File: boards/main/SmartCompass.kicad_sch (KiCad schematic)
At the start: 21 parts, among them J1 SWD HEADER, J2 EXPANSION, U1 BMD-340-A-R, U2 S25FL064LABNFI043, X1 USB4085-GF-A, Y1 32.768KHZ

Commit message: Fix missing/incorrect digikey numbers
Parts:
- R3, R5: DigiKey_PN (none) -> 311-27.0HRCT-ND
- R6, R7: DigiKey_PN (none) -> 311-4.70KHRCT-ND
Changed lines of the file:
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@@
 			)
 		)
+    (property "DigiKey_PN" "311-4.70KHRCT-ND" (at 128.27 92.71 0)
+      (effects (font (size 1.27 1.27)) (hide yes))
+    )
 		(pin "1"
 		)
@@
 			)
 		)
+    (property "DigiKey_PN" "311-27.0HRCT-ND" (at 254.0 77.47 0)
+      (effects (font (size 1.27 1.27)) (hide yes))
+    )
 		(pin "2"
 		)
@@
 			)
 		)
+    (property "DigiKey_PN" "311-4.70KHRCT-ND" (at 128.27 95.25 0)
+      (effects (font (size 1.27 1.27)) (hide yes))
+    )
 		(pin "1"
 		)
@@
 			)
 		)
+    (property "DigiKey_PN" "311-27.0HRCT-ND" (at 254.0 82.55 0)
+      (effects (font (size 1.27 1.27)) (hide yes))
+    )
 		(pin "2"
 		)

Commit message: Use proper flash footprint and model. Also swap out deprecated resistor on the main board
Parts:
- R1, R2, R4: DigiKey_PN 311-5.10KHRCT-ND -> P5.10KHCT-ND; MPN RC0603FR-075K1L -> ERJ-3EKF5101V; Manufacturer YAGEO -> Panasonic
- U2: footprint Package_DFN_QFN:DFN-8-1EP_4x4mm_P0.8mm_EP2.3x3.24mm -> smart_compass:SON80P400X400X60-9N
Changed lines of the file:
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@@
 			)
 		)
-		(property "Datasheet" "https://yageogroup.com/content/datasheet/asset/file/PYU-RC_GROUP_51_ROHS_L"
+		(property "Datasheet" "https://industrial.panasonic.com/cdbs/www-data/pdf/RDA0000/AOA0000C304.pdf"
 			(at 256.54 68.58 0)
 			(hide yes)
@@
 			)
 		)
-		(property "MPN" "RC0603FR-075K1L"
+		(property "MPN" "ERJ-3EKF5101V"
 			(at 256.54 68.58 0)
 			(hide yes)
@@
 			)
 		)
-		(property "Manufacturer" "YAGEO"
+		(property "Manufacturer" "Panasonic"
 			(at 256.54 68.58 0)
 			(hide yes)
@@
 			)
 		)
-		(property "DigiKey_PN" "311-5.10KHRCT-ND"
+		(property "DigiKey_PN" "P5.10KHCT-ND"
 			(at 256.54 68.58 0)
 			(hide yes)
@@
 			)
 		)
-    (property "DigiKey_PN" "311-4.70KHRCT-ND" (at 128.27 92.71 0)
-      (effects (font (size 1.27 1.27)) (hide yes))
-    )
+		(property "DigiKey_PN" "311-4.70KHRCT-ND"
+			(at 128.27 92.71 0)
+			(hide yes)
+			(show_name no)
+			(do_not_autoplace no)
+			(effects
+				(font
+					(size 1.27 1.27)
+				)
+			)
+		)
 		(pin "1"
 		)
@@
 			)
 		)
-    (property "DigiKey_PN" "311-27.0HRCT-ND" (at 254.0 77.47 0)
-      (effects (font (size 1.27 1.27)) (hide yes))
-    )
+		(property "DigiKey_PN" "311-27.0HRCT-ND"
+			(at 254 77.47 0)
+			(hide yes)
+			(show_name no)
+			(do_not_autoplace no)
+			(effects
+				(font
+					(size 1.27 1.27)
+				)
+			)
+		)
 		(pin "2"
 		)
@@
 			)
 		)
-		(property "Datasheet" "https://yageogroup.com/content/datasheet/asset/file/PYU-RC_GROUP_51_ROHS_L"
+		(property "Datasheet" "https://industrial.panasonic.com/cdbs/www-data/pdf/RDA0000/AOA0000C304.pdf"
 			(at 203.2 82.55 0)
 			(hide yes)
@@
 			)
 		)
-		(property "MPN" "RC0603FR-075K1L"
+		(property "MPN" "ERJ-3EKF5101V"
 			(at 203.2 82.55 0)
 			(hide yes)
@@
 			)
 		)
-		(property "Manufacturer" "YAGEO"
+		(property "Manufacturer" "Panasonic"
 			(at 203.2 82.55 0)
 			(hide yes)
@@
 			)
 		)
-		(property "DigiKey_PN" "311-5.10KHRCT-ND"
+		(property "DigiKey_PN" "P5.10KHCT-ND"
 			(at 203.2 82.55 0)
 			(hide yes)
@@
 			)
 		)
-		(property "Manufacturer" "Abracon"
-			(at 54.61 50.8 0)
-			(hide yes)
-			(show_name no)
-			(do_not_autoplace no)
-			(effects
-				(font
-					(size 1.27 1.27)
-				)
-				(justify bottom)
-			)
-		)
 		(property "MPN" "ABS07-32.768KHZ-7-T"
 			(at 54.61 50.8 90)
@@
 			)
 		)
-    (property "DigiKey_PN" "311-4.70KHRCT-ND" (at 128.27 95.25 0)
-      (effects (font (size 1.27 1.27)) (hide yes))
-    )
+		(property "DigiKey_PN" "311-4.70KHRCT-ND"
+			(at 128.27 95.25 0)
+			(hide yes)
+			(show_name no)
+			(do_not_autoplace no)
+			(effects
+				(font
+					(size 1.27 1.27)
+				)
+			)
+		)
 		(pin "1"
 		)
@@
 			)
 		)
-		(property "Datasheet" "https://yageogroup.com/content/datasheet/asset/file/PYU-RC_GROUP_51_ROHS_L"
+		(property "Datasheet" "https://industrial.panasonic.com/cdbs/www-data/pdf/RDA0000/AOA0000C304.pdf"
 			(at 256.54 71.12 0)
 			(hide yes)
@@
 			)
 		)
-		(property "MPN" "RC0603FR-075K1L"
+		(property "MPN" "ERJ-3EKF5101V"
 			(at 256.54 71.12 0)
 			(hide yes)
@@
 			)
 		)
-		(property "Manufacturer" "YAGEO"
+		(property "Manufacturer" "Panasonic"
 			(at 256.54 71.12 0)
 			(hide yes)
@@
 			)
 		)
-		(property "DigiKey_PN" "311-5.10KHRCT-ND"
+		(property "DigiKey_PN" "P5.10KHCT-ND"
 			(at 256.54 71.12 0)
 			(hide yes)
@@
 			)
 		)
-		(property "Footprint" "Package_DFN_QFN:DFN-8-1EP_4x4mm_P0.8mm_EP2.3x3.24mm"
+		(property "Footprint" "smart_compass:SON80P400X400X60-9N"
 			(at 248.92 146.05 0)
 			(hide yes)
@@
 			)
 		)
-		(property "Manufacturer" "Infineon Technologies"
-			(at 248.92 146.05 0)
-			(hide yes)
-			(show_name no)
-			(do_not_autoplace no)
-			(effects
-				(font
-					(size 1.27 1.27)
-				)
-				(justify bottom)
-			)
-		)
 		(property "MPN" "S25FL064LABNFI043"
 			(at 248.92 146.05 0)
@@
 			)
 		)
-    (property "DigiKey_PN" "311-27.0HRCT-ND" (at 254.0 82.55 0)
-      (effects (font (size 1.27 1.27)) (hide yes))
-    )
+		(property "DigiKey_PN" "311-27.0HRCT-ND"
+			(at 254 82.55 0)
+			(hide yes)
+			(show_name no)
+			(do_not_autoplace no)
+			(effects
+				(font
+					(size 1.27 1.27)
+				)
+			)
+		)
 		(pin "2"
 		)

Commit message: Grab missing footprints and models, and assign them to symbols
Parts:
- U1: footprint (none) -> smart_compass:RIGADO_BMD-340-A-R
- X1: footprint (none) -> smart_compass:GCT_USB4085-GF-A_REVA4
- Y1: footprint (none) -> smart_compass:XTAL_ABS07-32.768KHZ-7-T
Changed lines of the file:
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@@
 			)
 		)
-		(property "Footprint" ""
+		(property "Footprint" "smart_compass:RIGADO_BMD-340-A-R"
 			(at 97.79 69.85 0)
 			(hide yes)
@@
 			)
 		)
-		(property "Footprint" ""
+		(property "Footprint" "smart_compass:XTAL_ABS07-32.768KHZ-7-T"
 			(at 54.61 50.8 0)
 			(hide yes)
@@
 			)
 		)
-		(property "Footprint" ""
+		(property "Footprint" "smart_compass:GCT_USB4085-GF-A_REVA4"
 			(at 236.22 82.55 0)
 			(hide yes)

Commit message: replace capacitor that's in danger of being a bottleneck
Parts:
- C1, C2: DigiKey_PN 1276-6456-1-ND -> 445-6970-1-ND; MPN CL21A106KPFNNNG -> CGA4J3X5R1A106K125AB; Manufacturer Samsung Electro-Mechanics -> TDK; PRICE 0.07 -> 0.24
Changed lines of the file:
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@@
 			)
 		)
-		(property "Datasheet" "https://media.digikey.com/pdf/Data%20Sheets/Samsung%20PDFs/CL_Series_MLCC_ds.pdf"
+		(property "Datasheet" "https://product.tdk.com/system/files/dam/doc/product/capacitor/ceramic/mlcc/catalog/mlcc_automotive_general_en.pdf"
 			(at 127 26.67 0)
 			(hide yes)
@@
 			)
 		)
-		(property "MPN" "CL21A106KPFNNNG"
+		(property "MPN" "CGA4J3X5R1A106K125AB"
 			(at 127 26.67 90)
 			(hide yes)
@@
 			)
 		)
-		(property "PRICE" "0.07"
+		(property "PRICE" "0.24"
 			(at 127 26.67 90)
 			(hide yes)
@@
 			)
 		)
-		(property "Manufacturer" "Samsung Electro-Mechanics"
+		(property "Manufacturer" "TDK"
 			(at 127 26.67 0)
 			(hide yes)
@@
 			)
 		)
-		(property "DigiKey_PN" "1276-6456-1-ND"
+		(property "DigiKey_PN" "445-6970-1-ND"
 			(at 127 26.67 0)
 			(hide yes)
@@
 			)
 		)
-		(property "Datasheet" "https://media.digikey.com/pdf/Data%20Sheets/Samsung%20PDFs/CL_Series_MLCC_ds.pdf"
+		(property "Datasheet" "https://product.tdk.com/system/files/dam/doc/product/capacitor/ceramic/mlcc/catalog/mlcc_automotive_general_en.pdf"
 			(at 138.43 26.67 0)
 			(hide yes)
@@
 			)
 		)
-		(property "MPN" "CL21A106KPFNNNG"
+		(property "MPN" "CGA4J3X5R1A106K125AB"
 			(at 138.43 26.67 90)
 			(hide yes)
@@
 			)
 		)
-		(property "PRICE" "0.07"
+		(property "PRICE" "0.24"
 			(at 138.43 26.67 90)
 			(hide yes)
@@
 			)
 		)
-		(property "Manufacturer" "Samsung Electro-Mechanics"
+		(property "Manufacturer" "TDK"
 			(at 138.43 26.67 0)
 			(hide yes)
@@
 			)
 		)
-		(property "DigiKey_PN" "1276-6456-1-ND"
+		(property "DigiKey_PN" "445-6970-1-ND"
 			(at 138.43 26.67 0)
 			(hide yes)

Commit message: Fixing symbols
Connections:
- no-connect marks 13 -> 15
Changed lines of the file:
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@@
+	)
+	(no_connect
+		(at 113.03 87.63)
+	)
+	(no_connect
+		(at 113.03 85.09)
 	)
 	(no_connect
@@
 	(wire
 		(pts
+			(xy 78.74 33.02) (xy 68.58 33.02)
+		)
+		(stroke
+			(width 0)
+			(type default)
+		)
+	)
+	(wire
+		(pts
 			(xy 179.07 44.45) (xy 194.31 44.45)
 		)
@@
 		(pts
 			(xy 140.97 54.61) (xy 140.97 52.07)
-		)
-		(stroke
-			(width 0)
-			(type default)
-		)
-	)
-	(wire
-		(pts
-			(xy 78.74 33.02) (xy 68.58 33.02)
 		)
 		(stroke
@@
 	)
 	(label "uC_RESET"
-		(at 68.58 33.02 0)
+		(at 78.74 33.02 180)
 		(effects
 			(font
 				(size 1.2446 1.2446)
 			)
-			(justify left bottom)
-		)
-	)
+			(justify right bottom)
+		)
+	)

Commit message: Main board PCB layout. No mounting holes yet
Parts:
- removed J2: EXPANSION, Connector_PinHeader_2.54mm:PinHeader_1x08_P2.54mm_Vertical, symbol Connector_Generic:Conn_01x08
- C3, C4: value 12pF -> 10pF; DigiKey_PN 1276-1178-1-ND -> 1276-1139-1-ND; MPN CL05C120JB5NNNC -> CL05C100JB5NNNC; PRICE 0.00371 -> 0.00805
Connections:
- net User IO/DISP_BUSY: now also U1.63 (P1.14); no longer U1.57 (P1.01)
- net User IO/DISP_CS: now also U1.62 (P1.13); no longer U1.58 (P1.02)
- net User IO/DISP_DC: now also U1.61 (P1.12); no longer U1.59 (P1.03)
- net GPIO05: no longer names the net of U1.21 (P0.05)
- net GPIO17: no longer names the net of U1.35 (P0.17)
- net GPIO19: no longer names the net of U1.37 (P0.19)
- net GPIO20: no longer names the net of U1.38 (P0.20)
- no-connect marks 15 -> 17
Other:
- sheet User IO ports: added none; removed OSC1, OSC2
- note removed: "FUTURE EXPANSION BREAKOUT"

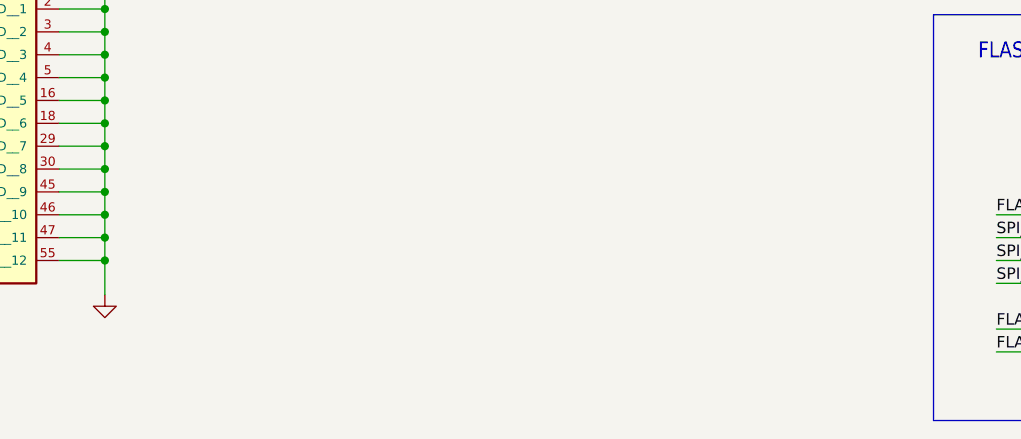
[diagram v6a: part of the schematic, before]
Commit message: add a spice sim definition for the main board
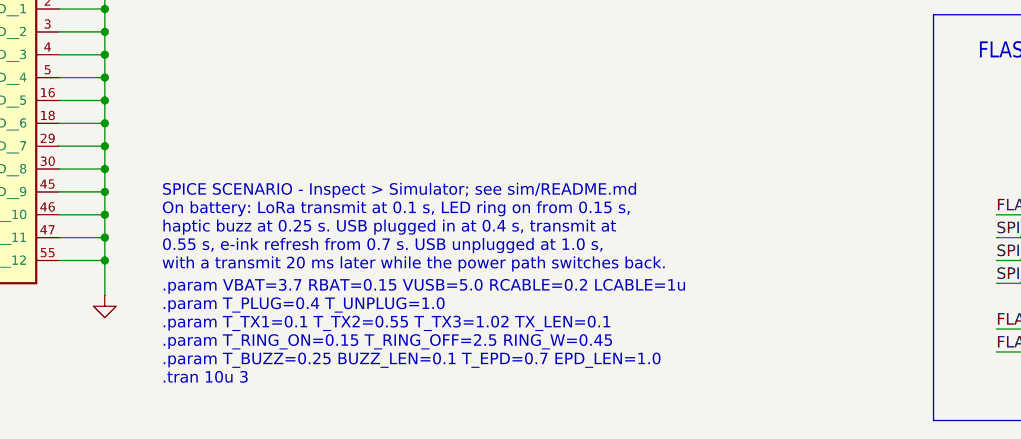
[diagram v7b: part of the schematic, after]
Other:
- note added: ".param VBAT=3.7 RBAT=0.15 VUSB=5.0 RCABLE=0.2 LCABLE=1u .param T_PLUG=0.4 T_UNPLUG=1.0 .param T_TX1=0.1 T_TX2=0.55 T_TX3=1.02 TX_LEN=0.1 .param T_RING_ON=0.15 T_RING_OFF=2.5 RING_W=0.45 .param T_BUZZ=0.25 BUZZ_LEN=0.1 T_EPD=0.7 EPD_LEN=1.0 .tran 10u 3"
- note added: "SPICE SCENARIO - Inspect > Simulator; see sim/README.md On battery: LoRa transmit at 0.1 s, LED ring on from 0.15 s, haptic buzz at 0.25 s. USB plugged in at 0.4 s, transmit at 0.55 s, e-ink refresh from 0.7 s. USB unplugged at 1.0 s, with a transmit 20 ms later while the power path switches back."
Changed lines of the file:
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@@
 		)
 	)
+	(text "SPICE SCENARIO - Inspect > Simulator; see sim/README.md\nOn battery: LoRa transmit at 0.1 s, LED ring on from 0.15 s,\nhaptic buzz at 0.25 s. USB plugged in at 0.4 s, transmit at\n0.55 s, e-ink refresh from 0.7 s. USB unplugged at 1.0 s,\nwith a transmit 20 ms later while the power path switches back."
+		(exclude_from_sim no)
+		(at 124.46 144.78 0)
+		(effects
+			(font
+				(size 1.27 1.27)
+			)
+			(justify left bottom)
+		)
+	)
 	(text "USB\n"
 		(exclude_from_sim no)
@@
 		)
 	)
+	(text ".param VBAT=3.7 RBAT=0.15 VUSB=5.0 RCABLE=0.2 LCABLE=1u\n.param T_PLUG=0.4 T_UNPLUG=1.0\n.param T_TX1=0.1 T_TX2=0.55 T_TX3=1.02 TX_LEN=0.1\n.param T_RING_ON=0.15 T_RING_OFF=2.5 RING_W=0.45\n.param T_BUZZ=0.25 BUZZ_LEN=0.1 T_EPD=0.7 EPD_LEN=1.0\n.tran 10u 3"
+		(exclude_from_sim no)
+		(at 124.46 157.48 0)
+		(effects
+			(font
+				(size 1.27 1.27)
+			)
+			(justify left bottom)
+		)
+	)
 	(junction
 		(at 247.65 82.55)
@@
 		(unit 1)
 		(body_style 1)
-		(exclude_from_sim no)
+		(exclude_from_sim yes)
 		(in_bom yes)
 		(on_board yes)
@@
 		(unit 1)
 		(body_style 1)
-		(exclude_from_sim no)
+		(exclude_from_sim yes)
 		(in_bom yes)
 		(on_board yes)
@@
 		(unit 1)
 		(body_style 1)
-		(exclude_from_sim no)
+		(exclude_from_sim yes)
 		(in_bom no)
 		(on_board yes)
@@
 			)
 		)
+		(property "Sim.Device" "SUBCKT"
+			(at 97.79 69.85 0)
+			(hide yes)
+			(show_name no)
+			(do_not_autoplace no)
+			(effects
+				(font
+					(size 1.27 1.27)
+				)
+			)
+		)
+		(property "Sim.Library" "${KIPRJMOD}/sim/fixtures.spice"
+			(at 97.79 69.85 0)
+			(hide yes)
+			(show_name no)
+			(do_not_autoplace no)
+			(effects
+				(font
+					(size 1.27 1.27)
+				)
+			)
+		)
+		(property "Sim.Name" "LOAD_NRF52840"
+			(at 97.79 69.85 0)
+			(hide yes)
+			(show_name no)
+			(do_not_autoplace no)
+			(effects
+				(font
+					(size 1.27 1.27)
+				)
+			)
+		)
+		(property "Sim.Pins" "17=VCC 66=VBUS 1=GND"
+			(at 97.79 69.85 0)
+			(hide yes)
+			(show_name no)
+			(do_not_autoplace no)
+			(effects
+				(font
+					(size 1.27 1.27)
+				)
+			)
+		)
 		(pin "1"
 		)
@@
 		(unit 1)
 		(body_style 1)
-		(exclude_from_sim no)
+		(exclude_from_sim yes)
 		(in_bom yes)
 		(on_board yes)
@@
 		(unit 1)
 		(body_style 1)
-		(exclude_from_sim no)
+		(exclude_from_sim yes)
 		(in_bom yes)
 		(on_board yes)
@@
 		(unit 1)
 		(body_style 1)
-		(exclude_from_sim no)
+		(exclude_from_sim yes)
 		(in_bom yes)
 		(on_board yes)
@@
 			)
 		)
+		(property "Sim.Device" "SUBCKT"
+			(at 248.92 146.05 0)
+			(hide yes)
+			(show_name no)
+			(do_not_autoplace no)
+			(effects
+				(font
+					(size 1.27 1.27)
+				)
+			)
+		)
+		(property "Sim.Library" "${KIPRJMOD}/sim/fixtures.spice"
+			(at 248.92 146.05 0)
+			(hide yes)
+			(show_name no)
+			(do_not_autoplace no)
+			(effects
+				(font
+					(size 1.27 1.27)
+				)
+			)
+		)
+		(property "Sim.Name" "LOAD_CONST"
+			(at 248.92 146.05 0)
+			(hide yes)
+			(show_name no)
+			(do_not_autoplace no)
+			(effects
+				(font
+					(size 1.27 1.27)
+				)
+			)
+		)
+		(property "Sim.Pins" "8=VDD 4=GND"
+			(at 248.92 146.05 0)
+			(hide yes)
+			(show_name no)
+			(do_not_autoplace no)
+			(effects
+				(font
+					(size 1.27 1.27)
+				)
+			)
+		)
+		(property "Sim.Params" "I=20u"
+			(at 248.92 146.05 0)
+			(hide yes)
+			(show_name no)
+			(do_not_autoplace no)
+			(effects
+				(font
+					(size 1.27 1.27)
+				)
+			)
+		)
 		(pin "1"
 		)
@@
 		(unit 1)
 		(body_style 1)
-		(exclude_from_sim no)
+		(exclude_from_sim yes)
 		(in_bom yes)
 		(on_board yes)
@@
 			(at 236.22 82.55 0)
 			(hide yes)
+			(show_name no)
+			(do_not_autoplace no)
+			(effects
+				(font
+					(size 1.27 1.27)
+				)
+			)
+		)
+		(property "Sim.Device" "SUBCKT"
+			(at 236.22 82.55 0)
+			(hide yes)
+			(show_name no)
+			(do_not_autoplace no)
+			(effects
+				(font
+					(size 1.27 1.27)
+				)
+			)
+		)
+		(property "Sim.Library" "${KIPRJMOD}/sim/fixtures.spice"
+			(at 236.22 82.55 0)
+			(hide yes)
+			(show_name no)
+			(do_not_autoplace no)
+			(effects
+				(font
+					(size 1.27 1.27)
+				)
+			)
+		)
+		(property "Sim.Name" "USB_HOST"
+			(at 236.22 82.55 0)
+			(hide yes)
+			(show_name no)
+			(do_not_autoplace no)
+			(effects
+				(font
+					(size 1.27 1.27)
+				)
+			)
+		)
+		(property "Sim.Pins" "A4=VBUS A1=GND"
+			(at 236.22 82.55 0)
+			(hide yes)

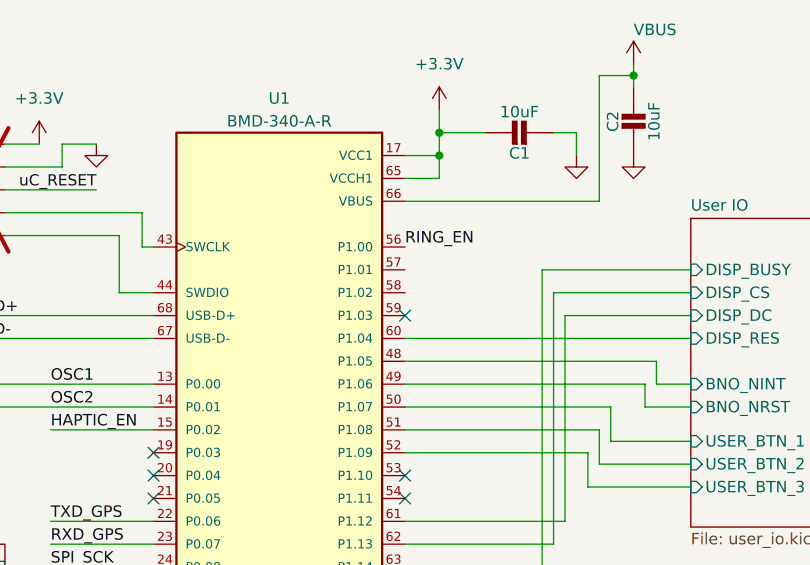
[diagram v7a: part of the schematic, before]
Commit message: Move the LED ring and haptic engine behind the charge controller, to prevent hot plug ringing from damaging things
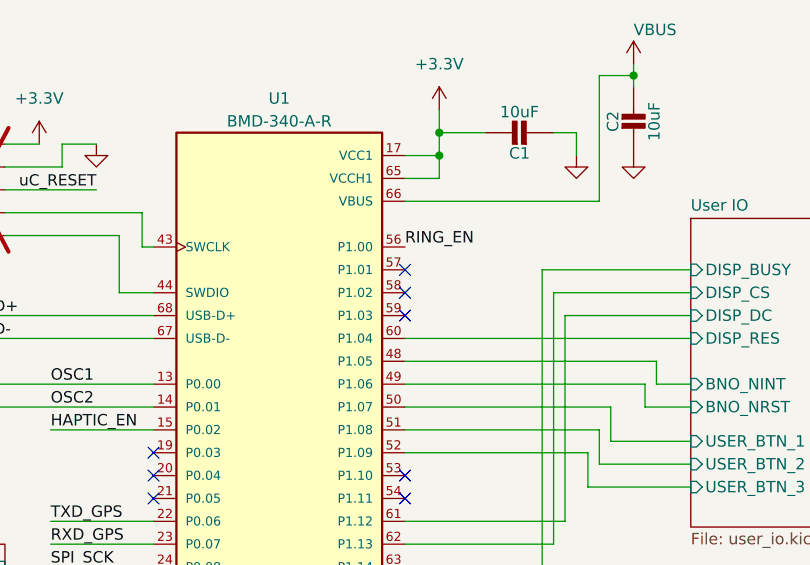
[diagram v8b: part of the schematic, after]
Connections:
- no-connect marks 17 -> 19
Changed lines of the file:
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@@
+	)
+	(no_connect
+		(at 113.03 44.45)
 	)
 	(no_connect
@@
 	)
 	(no_connect
+		(at 113.03 41.91)
+	)
+	(no_connect
